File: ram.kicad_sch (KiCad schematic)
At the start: 7 parts

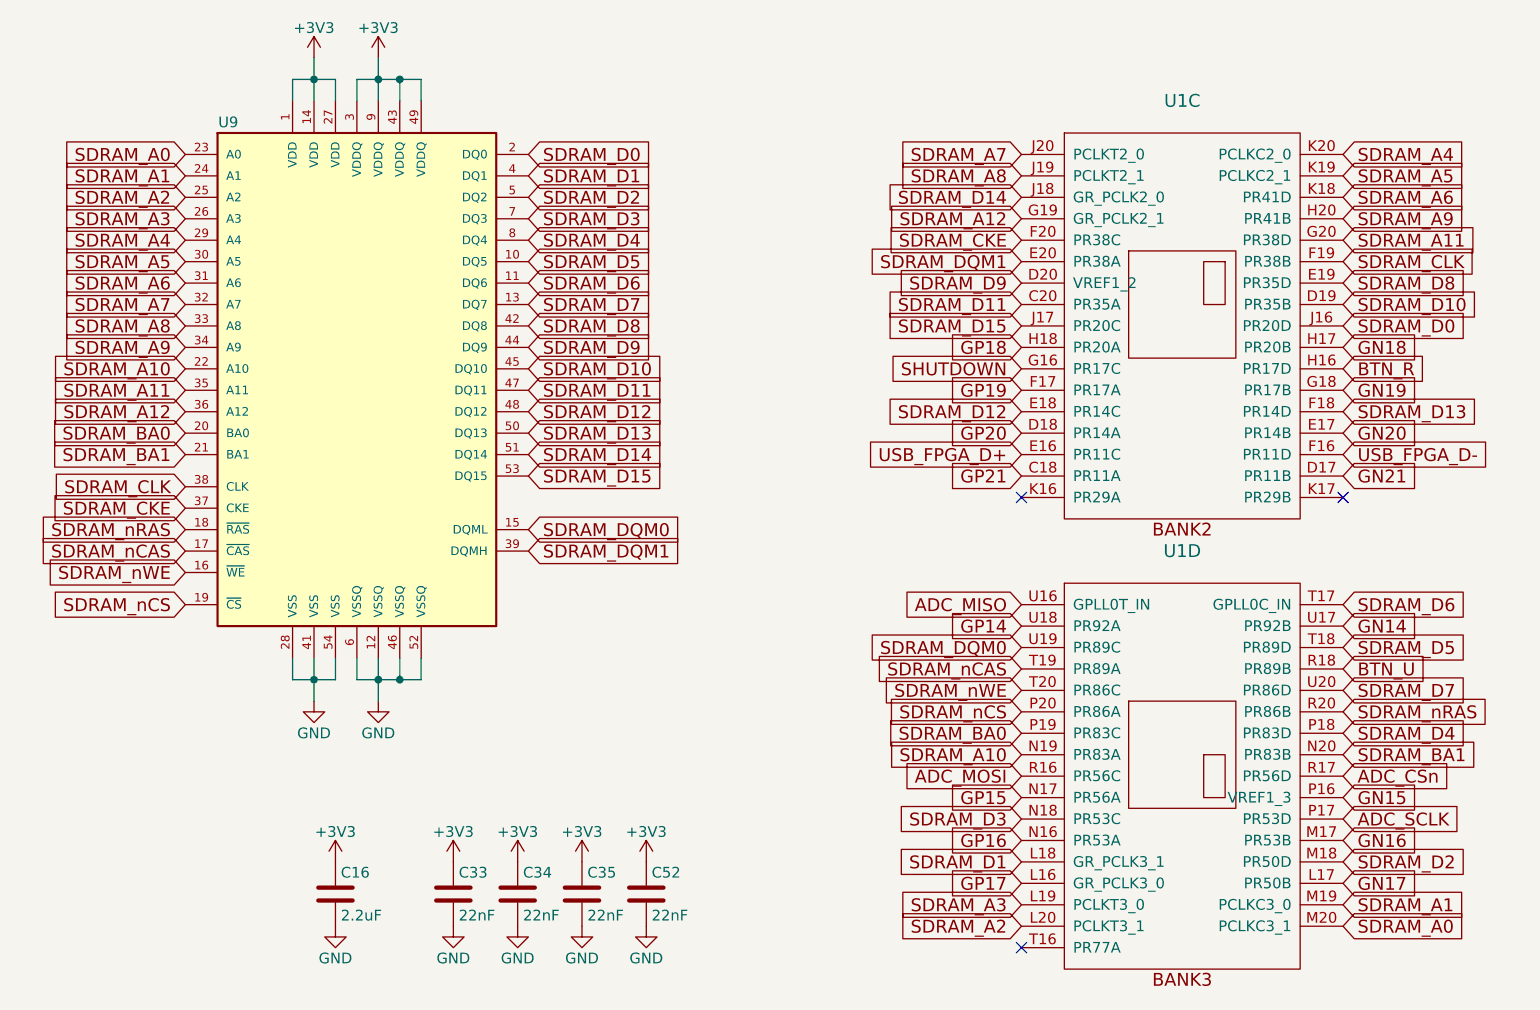
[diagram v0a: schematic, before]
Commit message: Full SerDes is now connected
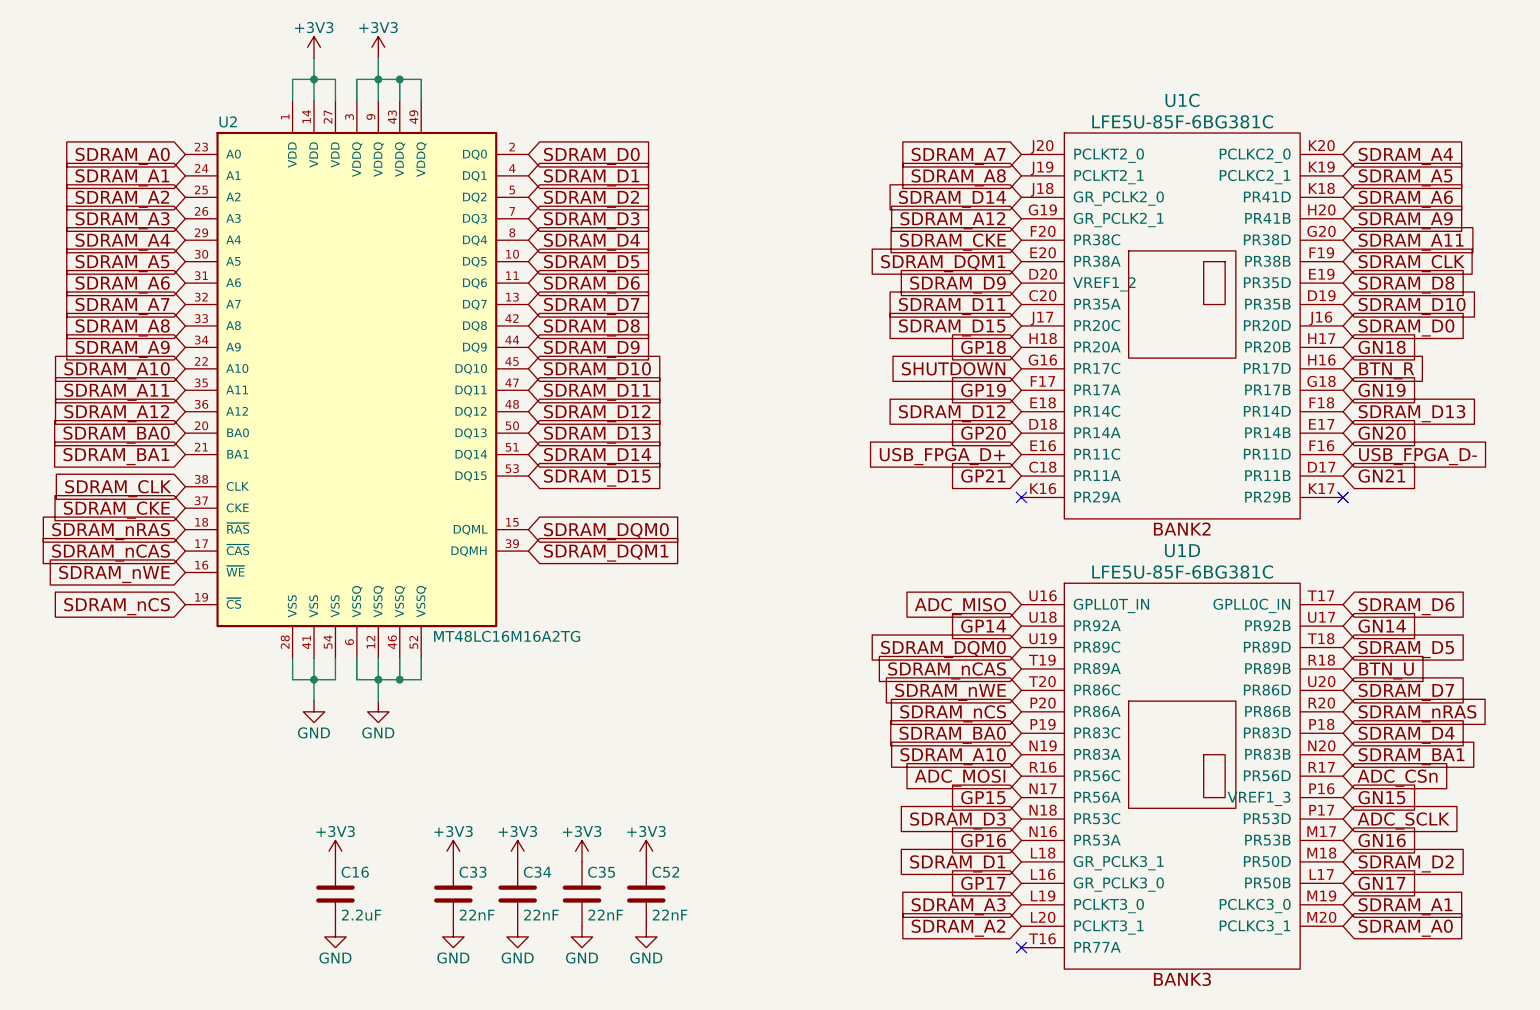
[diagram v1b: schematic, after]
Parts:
- U1: value (none) -> LFE5U-85F-6BG381C; footprint (none) -> lfe5bg381:BGA-381_pitch0.8mm_dia0.4mm; MNF1_URL (none) -> www.latticesemi.com
- U2: renamed from U9; value (none) -> MT48LC16M16A2TG; footprint (none) -> TSOP54:TSOP54
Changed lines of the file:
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@@
   (symbol (lib_id "mt48lc16m16a2tg:MT48LC16M16A2TG") (at 138.43 88.9 0) (unit 1)
     (in_bom yes) (on_board yes)
-    (property "Reference" "U9" (id 0) (at 123.19 58.42 0))
-    (property "Value" "" (id 1) (at 156.21 119.38 0))
-    (property "Footprint" "" (id 2) (at 138.43 88.9 0)
+    (property "Reference" "U2" (id 0) (at 123.19 58.42 0))
+    (property "Value" "MT48LC16M16A2TG" (id 1) (at 156.21 119.38 0))
+    (property "Footprint" "TSOP54:TSOP54" (id 2) (at 138.43 88.9 0)
       (effects (font (size 1.27 1.27) italic) hide)
     )
@@
   )
   (symbol (lib_id "lfe5bg381:LFE5UM-85F-6BG381C") (at 236.22 80.01 0) (unit 3)
-    (in_bom yes) (on_board yes)
+    (in_bom yes) (on_board no)
     (property "Reference" "U1" (id 0) (at 236.22 55.88 0)
       (effects (font (size 1.524 1.524)))
     )
-    (property "Value" "" (id 1) (at 236.22 58.42 0)
+    (property "Value" "LFE5U-85F-6BG381C" (id 1) (at 236.22 58.42 0)
       (effects (font (size 1.524 1.524)))
     )
-    (property "Footprint" "" (id 2) (at 209.55 55.88 0)
-      (effects (font (size 1.524 1.524)) hide)
-    )
-    (property "Datasheet" "http://www.latticesemi.com/~/media/LatticeSemi/Documents/DataSheets/ECP5/FPGA-DS-02012.pdf" (id 3) (at 209.55 55.88 0)
+    (property "Footprint" "lfe5bg381:BGA-381_pitch0.8mm_dia0.4mm" (id 2) (at 209.55 55.88 0)
+      (effects (font (size 1.524 1.524)) hide)
+    )
+    (property "Datasheet" "http://www.latticesemi.com/~/media/LatticeSemi/Documents/ApplicationNotes/EH/TN1261.pdf?document_id=50463" (id 3) (at 209.55 55.88 0)
       (effects (font (size 1.524 1.524)) hide)
     )
     (property "MPN" "LFE5U-85F-6BG381C" (id 4) (at 236.22 80.01 0)
+      (effects (font (size 1.524 1.524)) hide)
+    )
+    (property "MNF1_URL" "www.latticesemi.com" (id 5) (at 236.22 80.01 0)
       (effects (font (size 1.524 1.524)) hide)
     )
@@
   )
   (symbol (lib_id "lfe5bg381:LFE5UM-85F-6BG381C") (at 236.22 133.35 0) (unit 4)
-    (in_bom yes) (on_board yes)
+    (in_bom yes) (on_board no)
     (property "Reference" "U1" (id 0) (at 236.22 109.22 0)
       (effects (font (size 1.524 1.524)))
     )
-    (property "Value" "" (id 1) (at 236.22 111.76 0)
+    (property "Value" "LFE5U-85F-6BG381C" (id 1) (at 236.22 111.76 0)
       (effects (font (size 1.524 1.524)))
     )
-    (property "Footprint" "" (id 2) (at 209.55 109.22 0)
-      (effects (font (size 1.524 1.524)) hide)
-    )
-    (property "Datasheet" "http://www.latticesemi.com/~/media/LatticeSemi/Documents/DataSheets/ECP5/FPGA-DS-02012.pdf" (id 3) (at 209.55 109.22 0)
+    (property "Footprint" "lfe5bg381:BGA-381_pitch0.8mm_dia0.4mm" (id 2) (at 209.55 109.22 0)
+      (effects (font (size 1.524 1.524)) hide)
+    )
+    (property "Datasheet" "http://www.latticesemi.com/~/media/LatticeSemi/Documents/ApplicationNotes/EH/TN1261.pdf?document_id=50463" (id 3) (at 209.55 109.22 0)
       (effects (font (size 1.524 1.524)) hide)
     )
@@
       (effects (font (size 1.524 1.524)) hide)
     )
+    (property "MNF1_URL" "www.latticesemi.com" (id 5) (at 236.22 133.35 0)
+      (effects (font (size 1.524 1.524)) hide)
+    )
